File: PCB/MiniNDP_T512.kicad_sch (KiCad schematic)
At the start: 19 parts, among them J1 Conn_02x20_Odd_Even, U1 HC238, U2 HC4040, U3 HC573, U4 AS6C4008, U5 1G79, U6 2G00

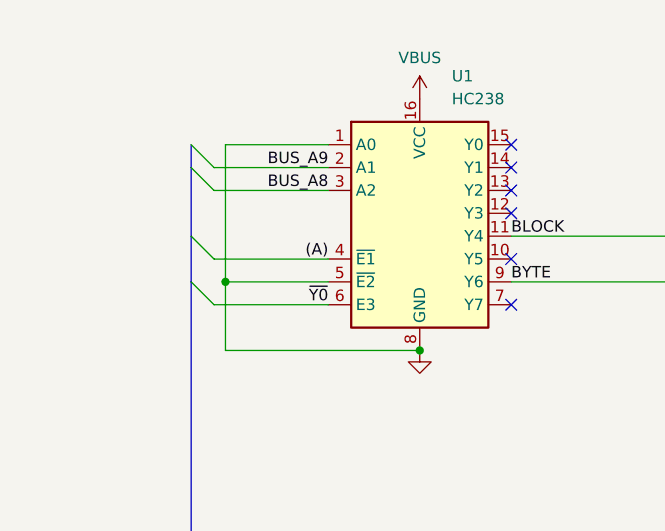
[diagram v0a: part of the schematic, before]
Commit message: T512 connect all gnd islands
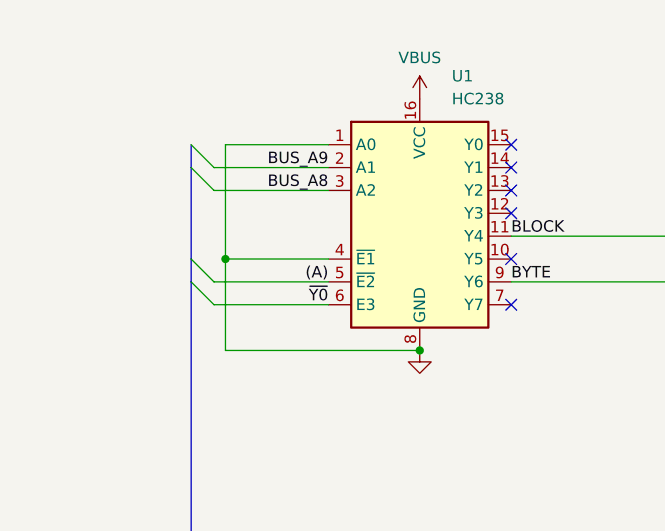
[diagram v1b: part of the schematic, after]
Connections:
- net (A): now also U1.5 (~{E2}); no longer U1.4 (~{E1})
- net GND: now also U1.4 (~{E1}); no longer U1.5 (~{E2})
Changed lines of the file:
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@@
 		(title "MiniNDP_T512")
 		(date "2026-08-05")
-		(rev "001")
+		(rev "002")
 		(company "Brian K. White - b.kenyon.w@gmail.com")
 		(comment 1 "github.com/bkw777/NODE_DATAPAC")
@@
 	)
 	(junction
-		(at 212.09 153.67)
+		(at 35.56 45.72)
 		(diameter 0)
 		(color 0 0 0 0)
 	)
 	(junction
-		(at 120.65 158.75)
+		(at 212.09 153.67)
 		(diameter 0)
 		(color 0 0 0 0)
 	)
 	(junction
-		(at 35.56 48.26)
+		(at 120.65 158.75)
 		(diameter 0)
 		(color 0 0 0 0)
@@
 	)
 	(bus_entry
-		(at 31.75 43.18)
+		(at 31.75 45.72)
 		(size 2.54 2.54)
 		(stroke
@@
 	(wire
 		(pts
-			(xy 35.56 48.26) (xy 46.99 48.26)
+			(xy 35.56 45.72) (xy 46.99 45.72)
 		)
 		(stroke
@@
 		)
 	)
-	(bus
-		(pts
-			(xy 31.75 43.18) (xy 31.75 48.26)
-		)
-		(stroke
-			(width 0)
-			(type default)
-		)
-	)
 	(wire
 		(pts
@@
 	(wire
 		(pts
-			(xy 34.29 45.72) (xy 46.99 45.72)
+			(xy 34.29 48.26) (xy 46.99 48.26)
 		)
 		(stroke
@@
 	(wire
 		(pts
-			(xy 35.56 33.02) (xy 35.56 48.26)
+			(xy 35.56 33.02) (xy 35.56 45.72)
 		)
 		(stroke
@@
 	(bus
 		(pts
+			(xy 31.75 45.72) (xy 31.75 48.26)
+		)
+		(stroke
+			(width 0)
+			(type default)
+		)
+	)
+	(bus
+		(pts
 			(xy 186.69 96.52) (xy 186.69 99.06)
 		)
@@
 		)
 	)
-	(wire
-		(pts
-			(xy 35.56 48.26) (xy 35.56 55.88)
-		)
-		(stroke
-			(width 0)
-			(type default)
-		)
-	)
 	(bus
 		(pts
@@
 	(bus
 		(pts
-			(xy 31.75 43.18) (xy 31.75 35.56)
+			(xy 31.75 35.56) (xy 31.75 45.72)
 		)
 		(stroke
@@
 	(wire
 		(pts
+			(xy 35.56 45.72) (xy 35.56 55.88)
+		)
+		(stroke
+			(width 0)
+			(type default)
+		)
+	)
+	(wire
+		(pts
 			(xy 133.35 124.46) (xy 146.05 124.46)
 		)
@@
 	)
 	(label "(A)"
-		(at 46.99 45.72 180)
+		(at 46.99 48.26 180)
 		(effects
 			(font

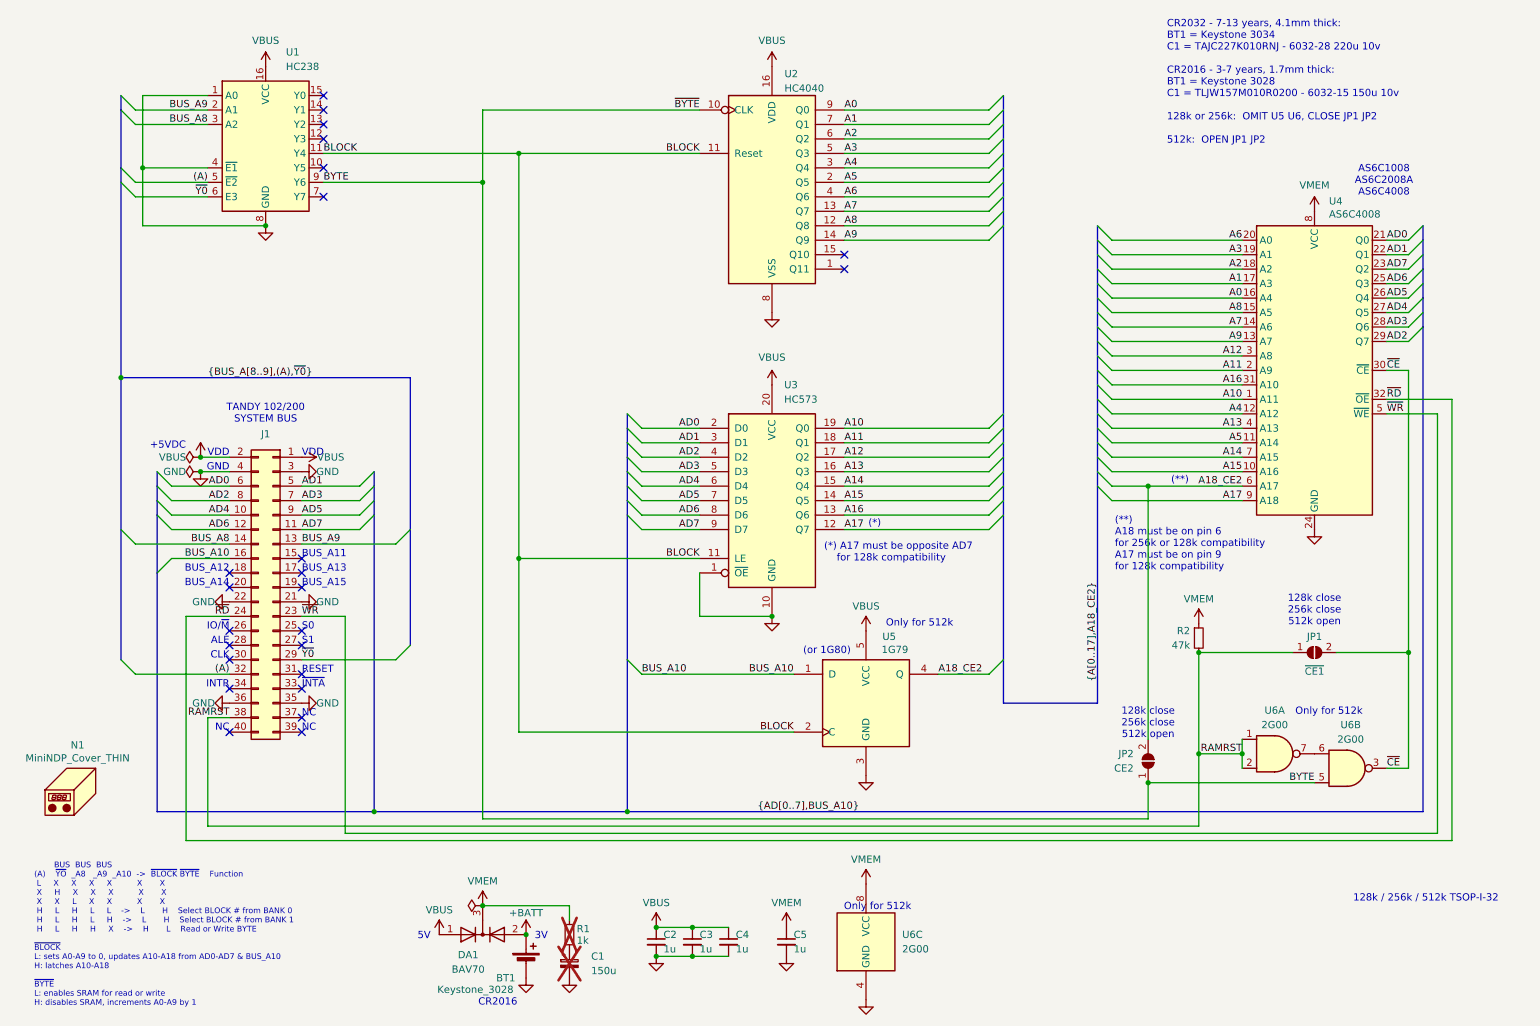
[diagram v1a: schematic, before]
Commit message: T512 power traces
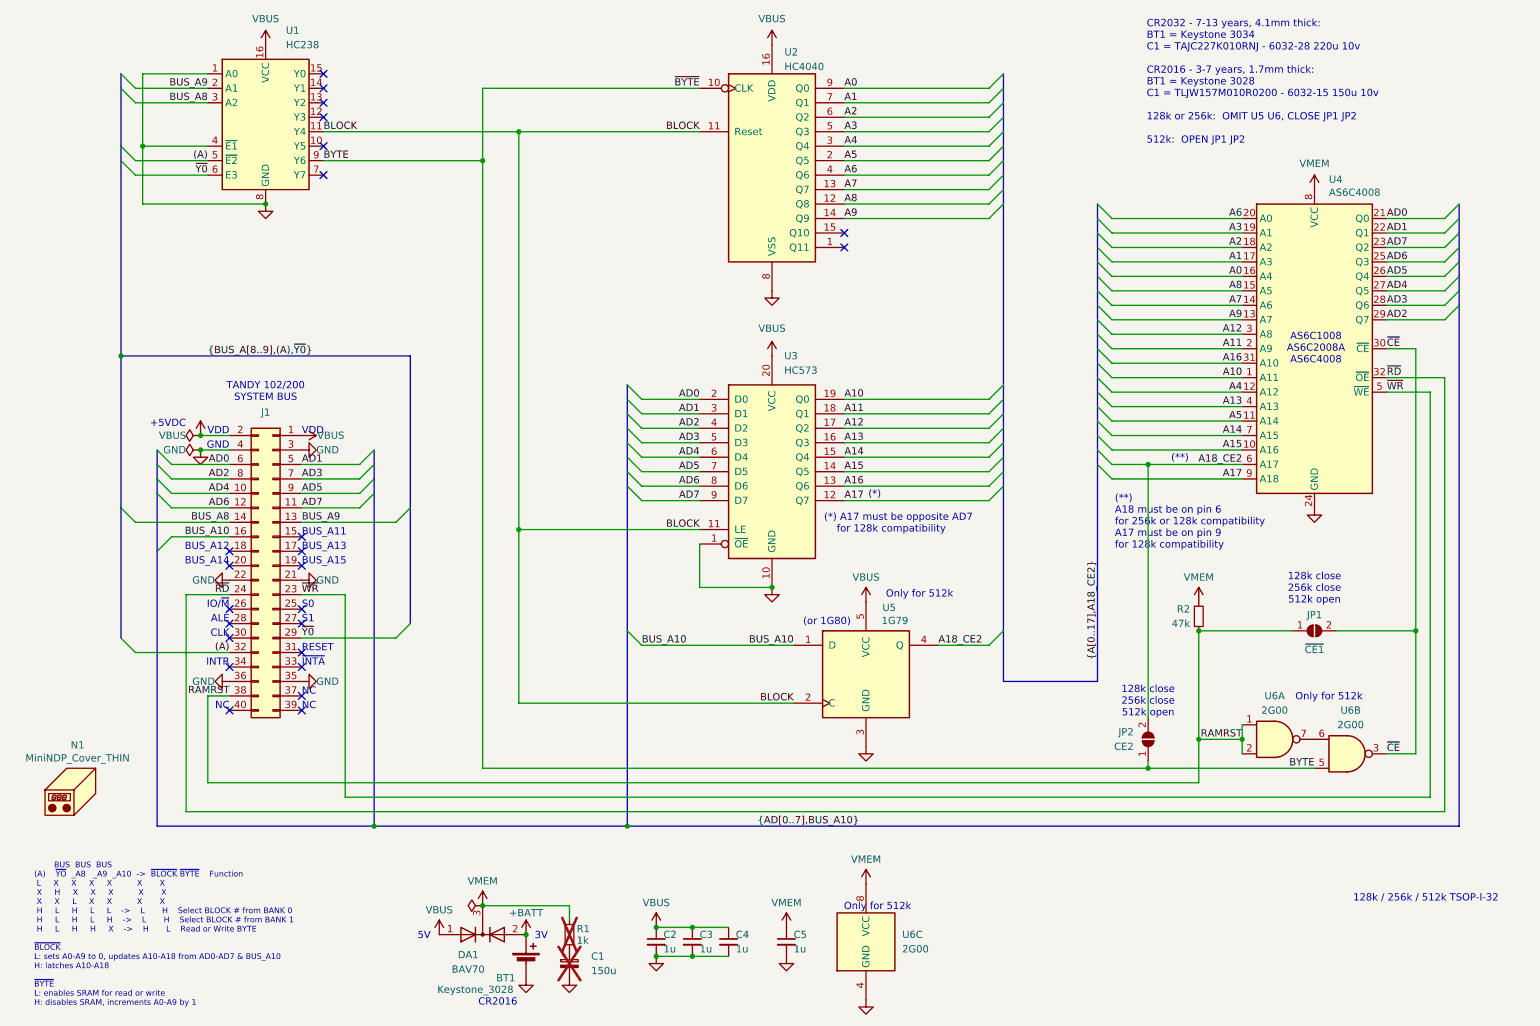
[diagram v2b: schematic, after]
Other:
- moved on the sheet: J1, JP1, JP2, R2, U1, U2, U3, U4, U5, U6A, U6B

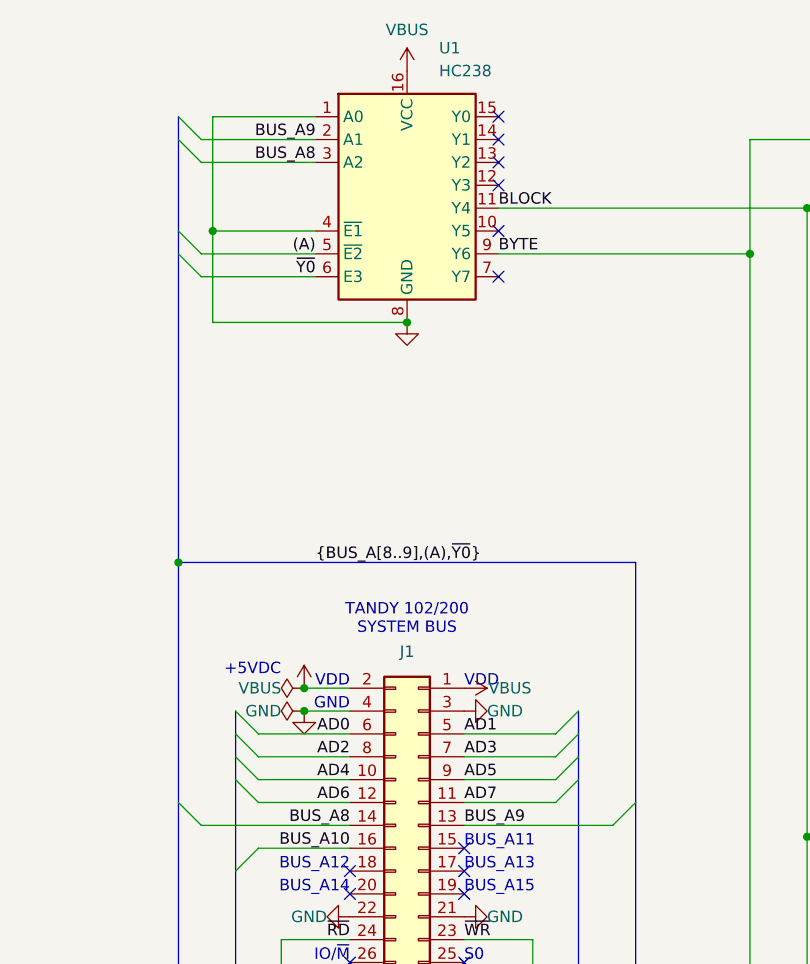
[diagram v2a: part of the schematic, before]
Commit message: M10c compact pcb & cover a little smaller & symmetrical
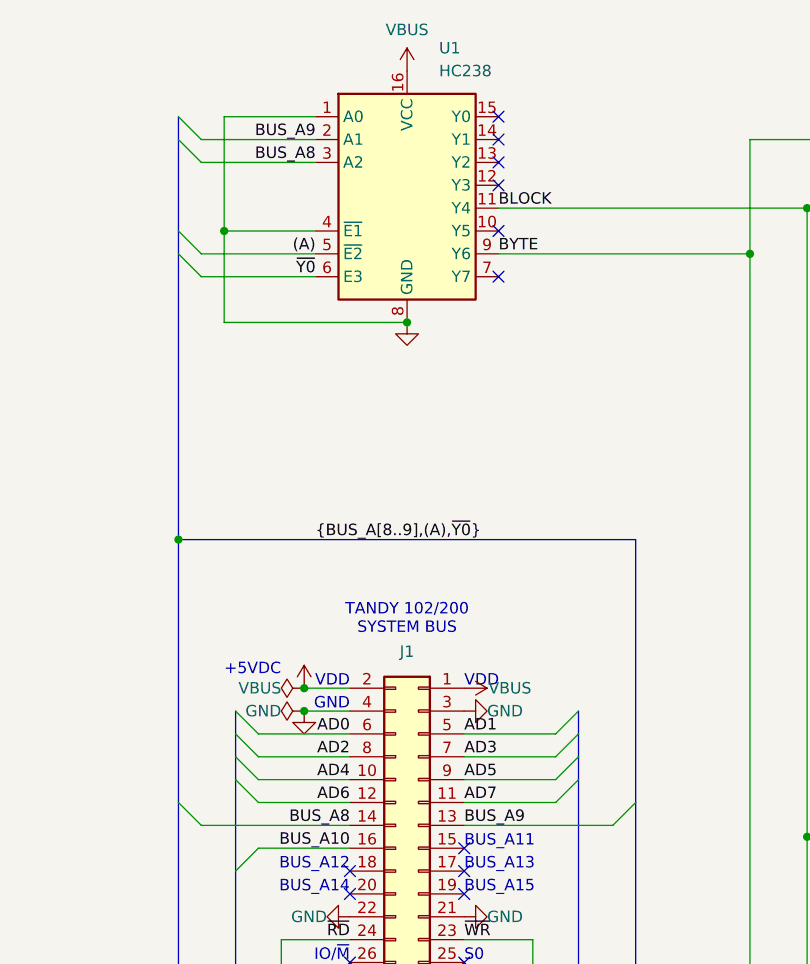
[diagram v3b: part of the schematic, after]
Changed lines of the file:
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@@
 	)
 	(junction
+		(at 36.83 41.91)
+		(diameter 0)
+		(color 0 0 0 0)
+	)
+	(junction
 		(at 45.72 92.71)
 		(diameter 0)
@@
 	)
 	(junction
-		(at 132.08 179.07)
+		(at 31.75 76.2)
 		(diameter 0)
 		(color 0 0 0 0)
 	)
 	(junction
-		(at 31.75 78.74)
+		(at 132.08 179.07)
 		(diameter 0)
 		(color 0 0 0 0)
@@
 		(color 0 0 0 0)
 	)
-	(junction
-		(at 35.56 41.91)
-		(diameter 0)
-		(color 0 0 0 0)
-	)
 	(no_connect
 		(at 67.31 34.29)
@@
 	(bus
 		(pts
+			(xy 31.75 76.2) (xy 31.75 105.41)
+		)
+		(stroke
+			(width 0)
+			(type default)
+		)
+	)
+	(bus
+		(pts
 			(xy 186.69 135.89) (xy 203.2 135.89)
 		)
@@
 	(wire
 		(pts
-			(xy 35.56 41.91) (xy 46.99 41.91)
-		)
-		(stroke
-			(width 0)
-			(type default)
-		)
-	)
-	(wire
-		(pts
 			(xy 228.6 143.51) (xy 228.6 146.05)
 		)
@@
 	(bus
 		(pts
-			(xy 82.55 78.74) (xy 82.55 105.41)
+			(xy 82.55 76.2) (xy 82.55 105.41)
 		)
 		(stroke
@@
 	(bus
 		(pts
-			(xy 31.75 78.74) (xy 31.75 105.41)
-		)
-		(stroke
-			(width 0)
-			(type default)
-		)
-	)
-	(bus
-		(pts
 			(xy 203.2 69.85) (xy 203.2 72.39)
 		)
@@
 	(wire
 		(pts
-			(xy 35.56 29.21) (xy 35.56 41.91)
+			(xy 36.83 29.21) (xy 36.83 41.91)
 		)
 		(stroke
@@
 		)
 	)
+	(wire
+		(pts
+			(xy 36.83 41.91) (xy 46.99 41.91)
+		)
+		(stroke
+			(width 0)
+			(type default)
+		)
+	)
 	(bus
 		(pts
@@
 	(wire
 		(pts
-			(xy 35.56 52.07) (xy 57.15 52.07)
+			(xy 36.83 52.07) (xy 57.15 52.07)
 		)
 		(stroke
@@
 	(bus
 		(pts
-			(xy 31.75 78.74) (xy 82.55 78.74)
+			(xy 31.75 76.2) (xy 82.55 76.2)
 		)
 		(stroke
@@
 	(wire
 		(pts
-			(xy 35.56 29.21) (xy 46.99 29.21)
+			(xy 36.83 29.21) (xy 46.99 29.21)
 		)
 		(stroke
@@
 	(bus
 		(pts
-			(xy 31.75 44.45) (xy 31.75 78.74)
+			(xy 31.75 44.45) (xy 31.75 76.2)
 		)
 		(stroke
@@
 	(wire
 		(pts
-			(xy 35.56 41.91) (xy 35.56 52.07)
+			(xy 36.83 41.91) (xy 36.83 52.07)
 		)
 		(stroke
@@
 	)
 	(label "{BUS_A[8..9],(A),~{Y0}}"
-		(at 46.99 78.74 0)
+		(at 46.99 76.2 0)
 		(effects
 			(font

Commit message: simplify covers, strengthen battery holders, silkscreen, readme
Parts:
- BT1: footprint 000_LOCAL:Keystone_3028_3034 -> 000_LOCAL:Keystone_3028_3034_bkw
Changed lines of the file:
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@@
 			)
 		)
-		(property "Footprint" "000_LOCAL:Keystone_3028_3034"
+		(property "Footprint" "000_LOCAL:Keystone_3028_3034_bkw"
 			(at 102.87 183.896 90)
 			(effects
@@
 		(on_board yes)
 		(dnp no)
-		(fields_autoplaced yes)
 		(property "Reference" "U6"
 			(at 234.315 138.43 0)
